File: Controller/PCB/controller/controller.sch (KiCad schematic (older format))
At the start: 8 parts

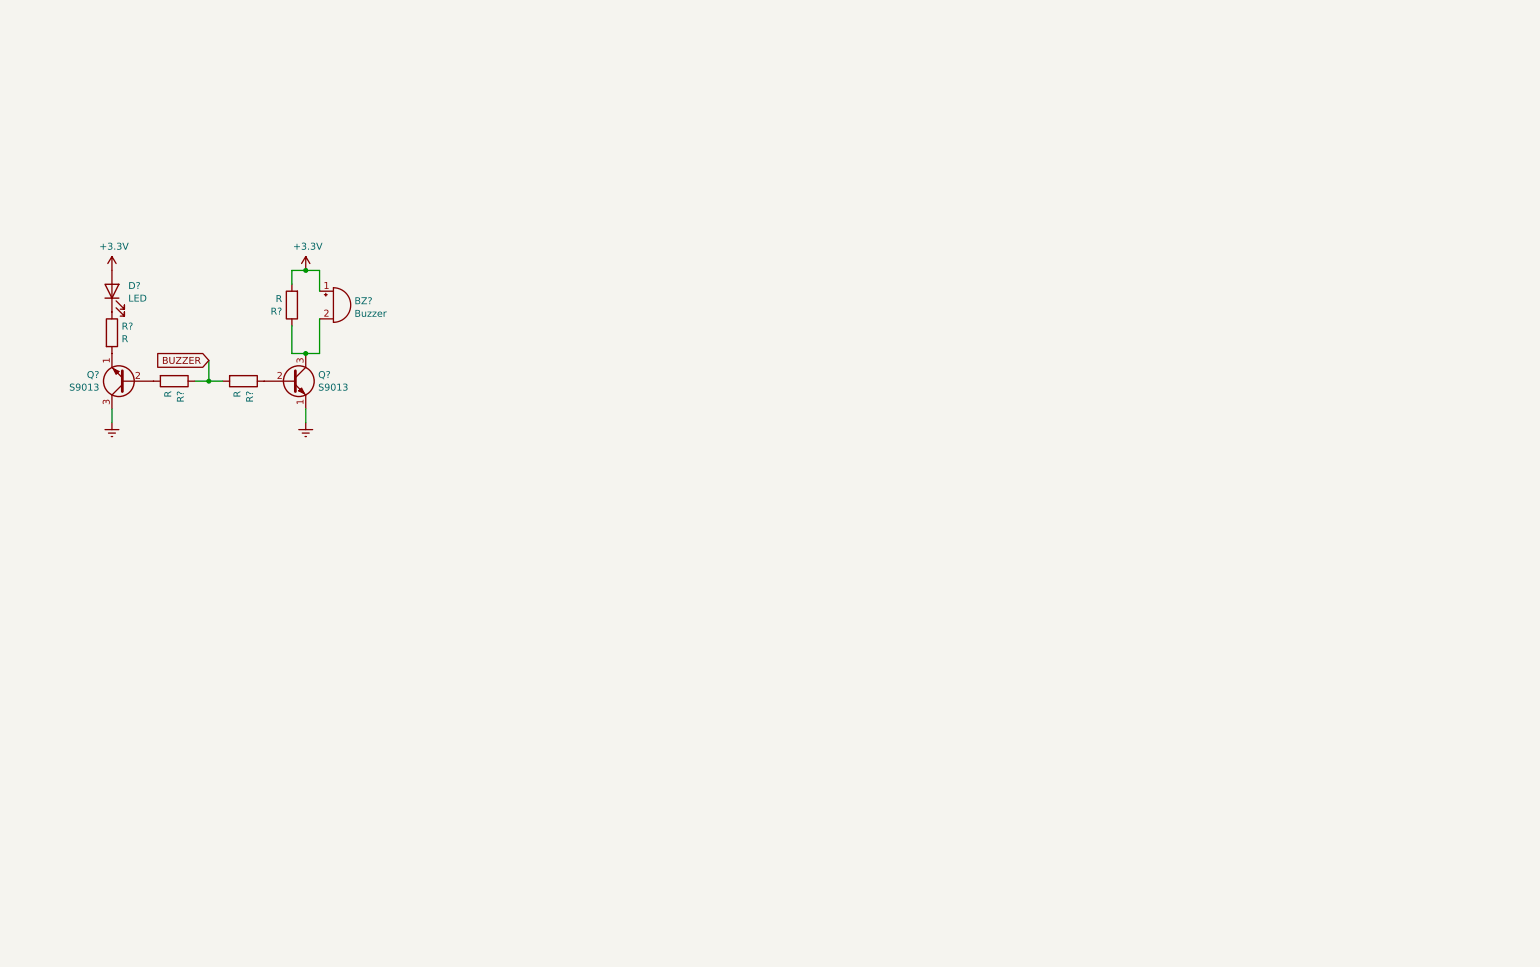
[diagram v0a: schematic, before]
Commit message: Add All inputs and Outputs to Circuit diagram
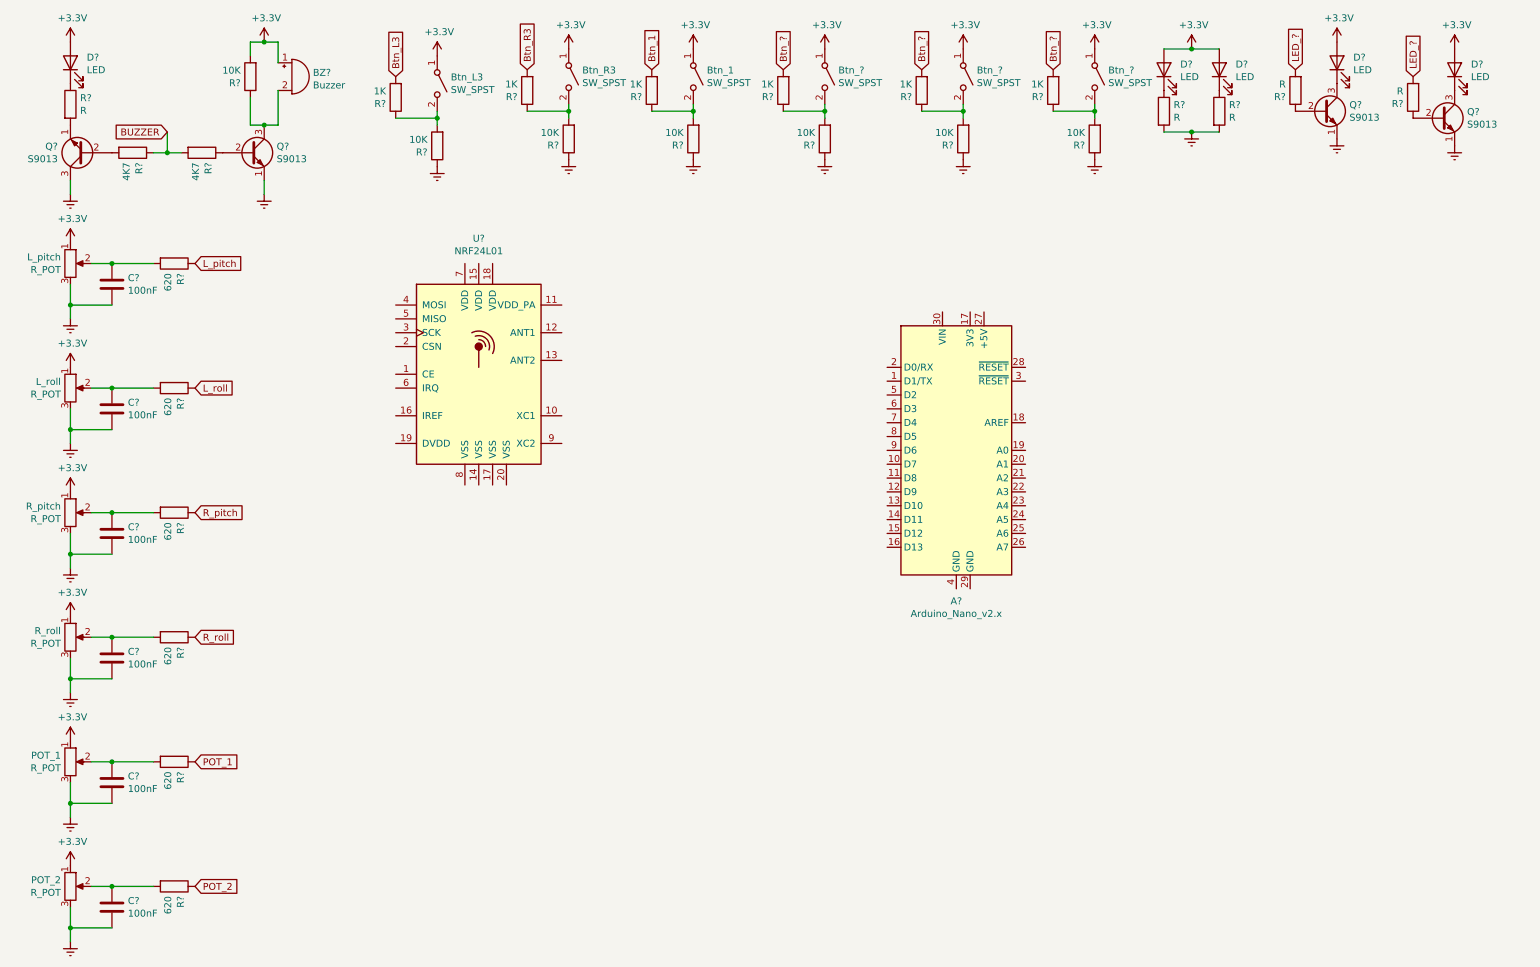
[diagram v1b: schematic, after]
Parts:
- added A?: Arduino_Nano_v2.x, Module:Arduino_Nano, symbol MCU_Module:Arduino_Nano_v2.x
- added Btn_1, Btn_? (x3), Btn_L3, Btn_R3: SW_SPST, symbol Switch:SW_SPST
- added C? (x6): 100nF, symbol Device:C
- added D? (x4): LED, symbol Device:LED
- added L_pitch, L_roll, POT_1, POT_2, R_pitch, R_roll: R_POT, symbol Device:R_POT
- added Q? (x2): S9013, Package_TO_SOT_THT:TO-39-3, symbol Transistor_BJT:2N2219
- added R? (x6): 620, symbol Device:R
- added R? (x6): 1K, symbol Device:R
- added R? (x6): 10K, symbol Device:R
- added R? (x4): R, symbol Device:R
- added U?: NRF24L01, Package_DFN_QFN:QFN-20-1EP_4x4mm_P0.5mm_EP2.5x2.5mm, symbol RF:NRF24L01
- R? (x2): value R -> 4K7
- R?: value R -> 10K
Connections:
- net +3V3: now also Btn_1.1 (A), Btn_?.1 (A), Btn_?.1 (A), Btn_?.1 (A), Btn_L3.1 (A), Btn_R3.1 (A), D?.2 (A), D?.2 (A), D?.2 (A), D?.2 (A), L_pitch.1, L_roll.1, POT_1.1, POT_2.1, R_pitch.1, R_roll.1
- net Earth: now also C?.2, C?.2, C?.2, C?.2, C?.2, C?.2, L_pitch.3, L_roll.3, POT_1.3, POT_2.3, Q?.1 (E), Q?.1 (E), R?.1, R?.1, R?.1, R?.1, R?.1, R?.1, R?.2, R?.2, R_pitch.3, R_roll.3
- new net: C?.1, L_pitch.2, R?.2
- new net: C?.1, L_roll.2, R?.2
- new net: C?.1, R?.2, R_pitch.2
- new net: C?.1, R?.2, R_roll.2
- new net: C?.1, POT_1.2, R?.2
- new net: C?.1, POT_2.2, R?.2
- new net: Btn_L3.2 (B), R?.1, R?.2
- new net: Btn_R3.2 (B), R?.1, R?.2
- new net: Btn_1.2 (B), R?.1, R?.2
- new net: Btn_?.2 (B), R?.1, R?.2 (x3)
- new net: D?.1 (K), R?.1 (x2)
- new net: D?.1 (K), Q?.3 (C) (x2)
- new net: Q?.2 (B), R?.1 (x2)
- new net Btn_1: R?.2
- new net Btn_?: R?.2, R?.2, R?.2
- new net Btn_L3: R?.2
- new net Btn_R3: R?.2
- new net LED_?: R?.2, R?.2
- new net L_pitch: R?.1
- new net L_roll: R?.1
- new net POT_1: R?.1
- new net POT_2: R?.1
- new net R_pitch: R?.1
- new net R_roll: R?.1
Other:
- moved on the sheet: BZ?, D?, Q?, R?

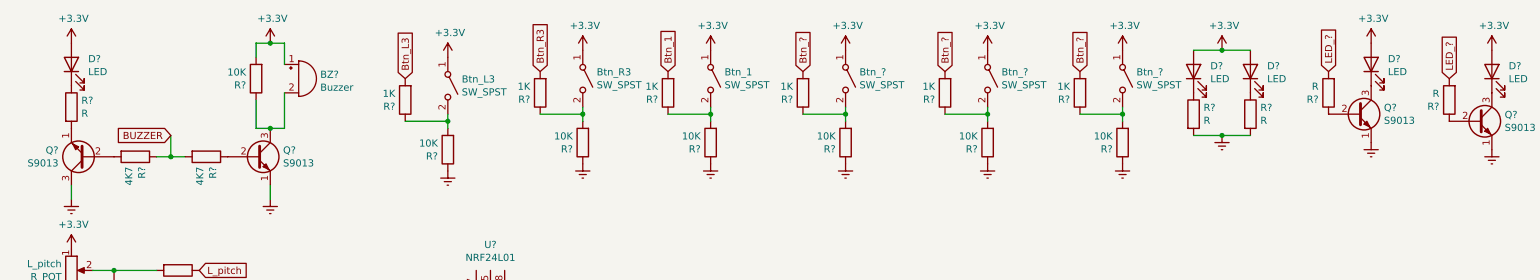
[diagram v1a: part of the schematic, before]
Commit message: Add Resistor Vals to the LEDs
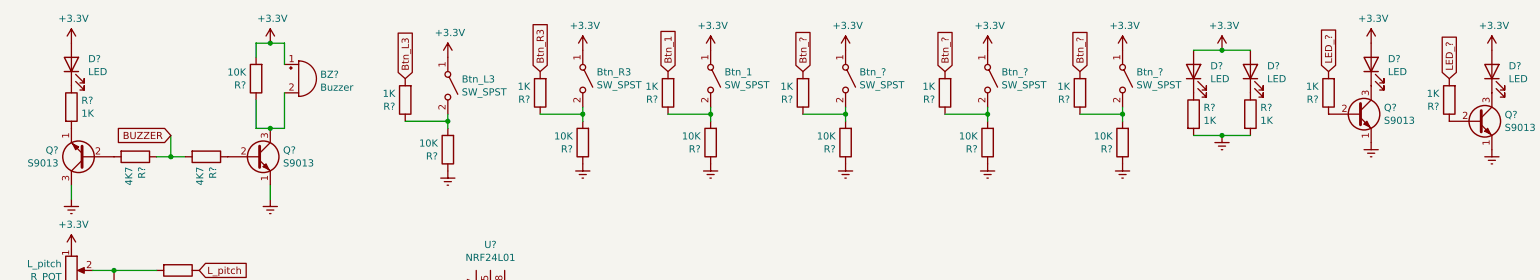
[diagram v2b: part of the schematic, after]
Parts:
- R? (x5): value R -> 1K
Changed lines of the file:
@@
 P 850 1150
 F 0 "R?" H 920 1196 50  0000 L CNN
-F 1 "R" H 920 1105 50  0000 L CNN
+F 1 "1K" H 920 1105 50  0000 L CNN
 F 2 "" V 780 1150 50  0001 C CNN
 F 3 "~" H 850 1150 50  0001 C CNN
@@
 P 8750 1200
 F 0 "R?" H 8820 1246 50  0000 L CNN
-F 1 "R" H 8820 1155 50  0000 L CNN
+F 1 "1K" H 8820 1155 50  0000 L CNN
 F 2 "" V 8680 1200 50  0001 C CNN
 F 3 "~" H 8750 1200 50  0001 C CNN
@@
 P 9150 1200
 F 0 "R?" H 9220 1246 50  0000 L CNN
-F 1 "R" H 9220 1155 50  0000 L CNN
+F 1 "1K" H 9220 1155 50  0000 L CNN
 F 2 "" V 9080 1200 50  0001 C CNN
 F 3 "~" H 9150 1200 50  0001 C CNN
@@
 P 9700 1050
 F 0 "R?" H 9770 1096 50  0000 L CNN
-F 1 "R" H 9770 1005 50  0000 L CNN
+F 1 "1K" H 9770 1005 50  0000 L CNN
 F 2 "" V 9630 1050 50  0001 C CNN
 F 3 "~" H 9700 1050 50  0001 C CNN
@@
 P 10550 1100
 F 0 "R?" H 10620 1146 50  0000 L CNN
-F 1 "R" H 10620 1055 50  0000 L CNN
+F 1 "1K" H 10620 1055 50  0000 L CNN
 F 2 "" V 10480 1100 50  0001 C CNN
 F 3 "~" H 10550 1100 50  0001 C CNN

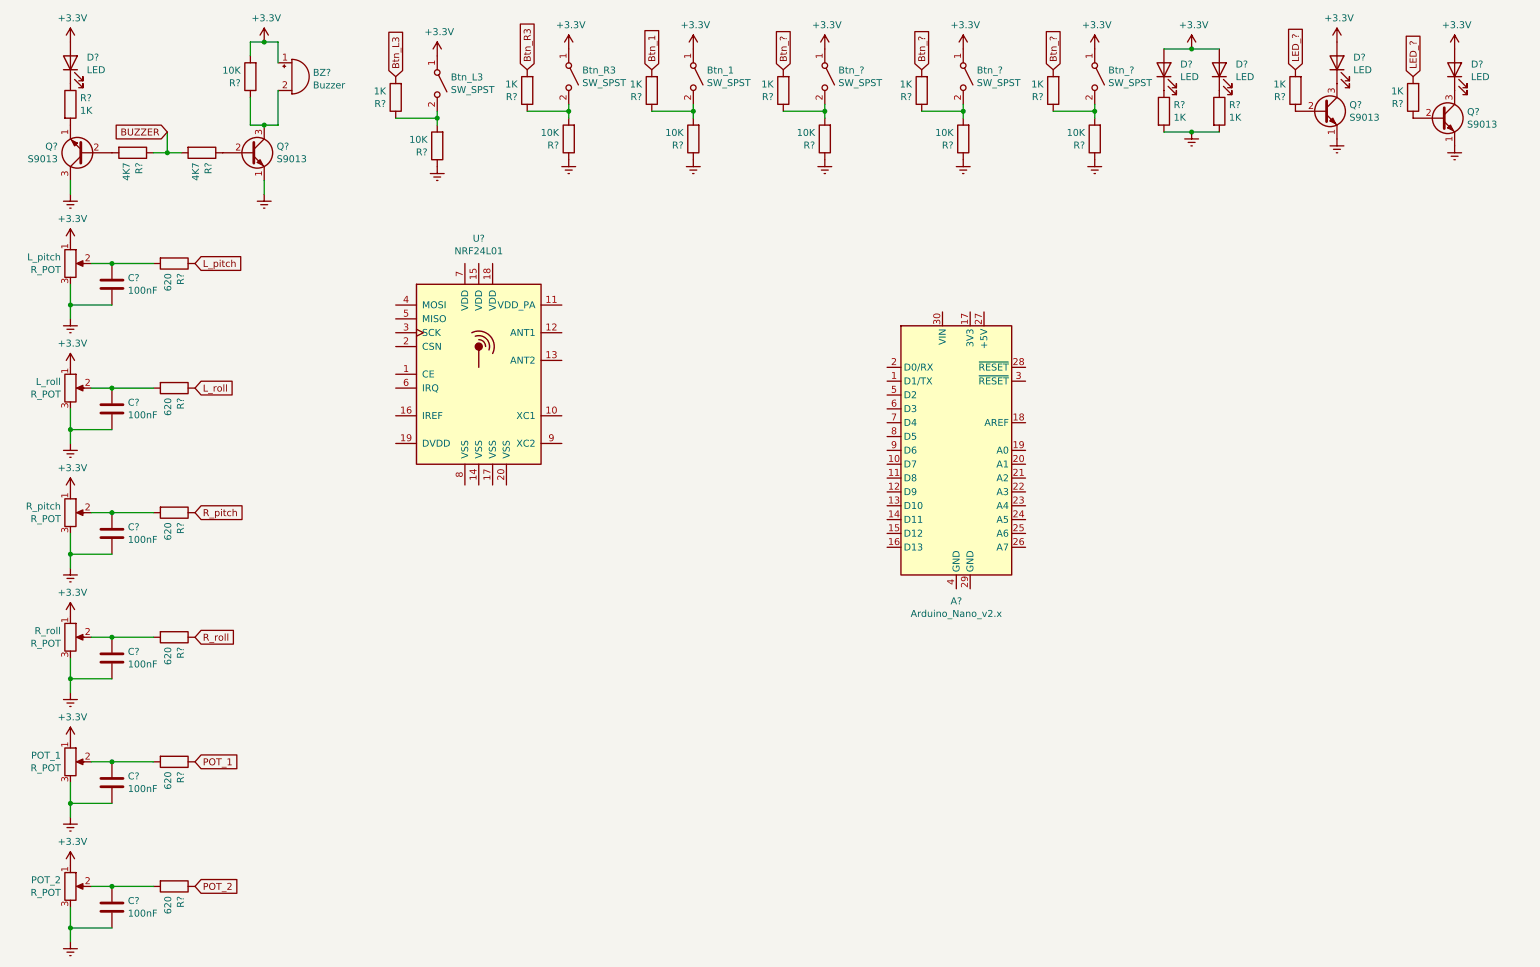
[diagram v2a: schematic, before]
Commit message: Add component pinouts and battery and voltage regulator
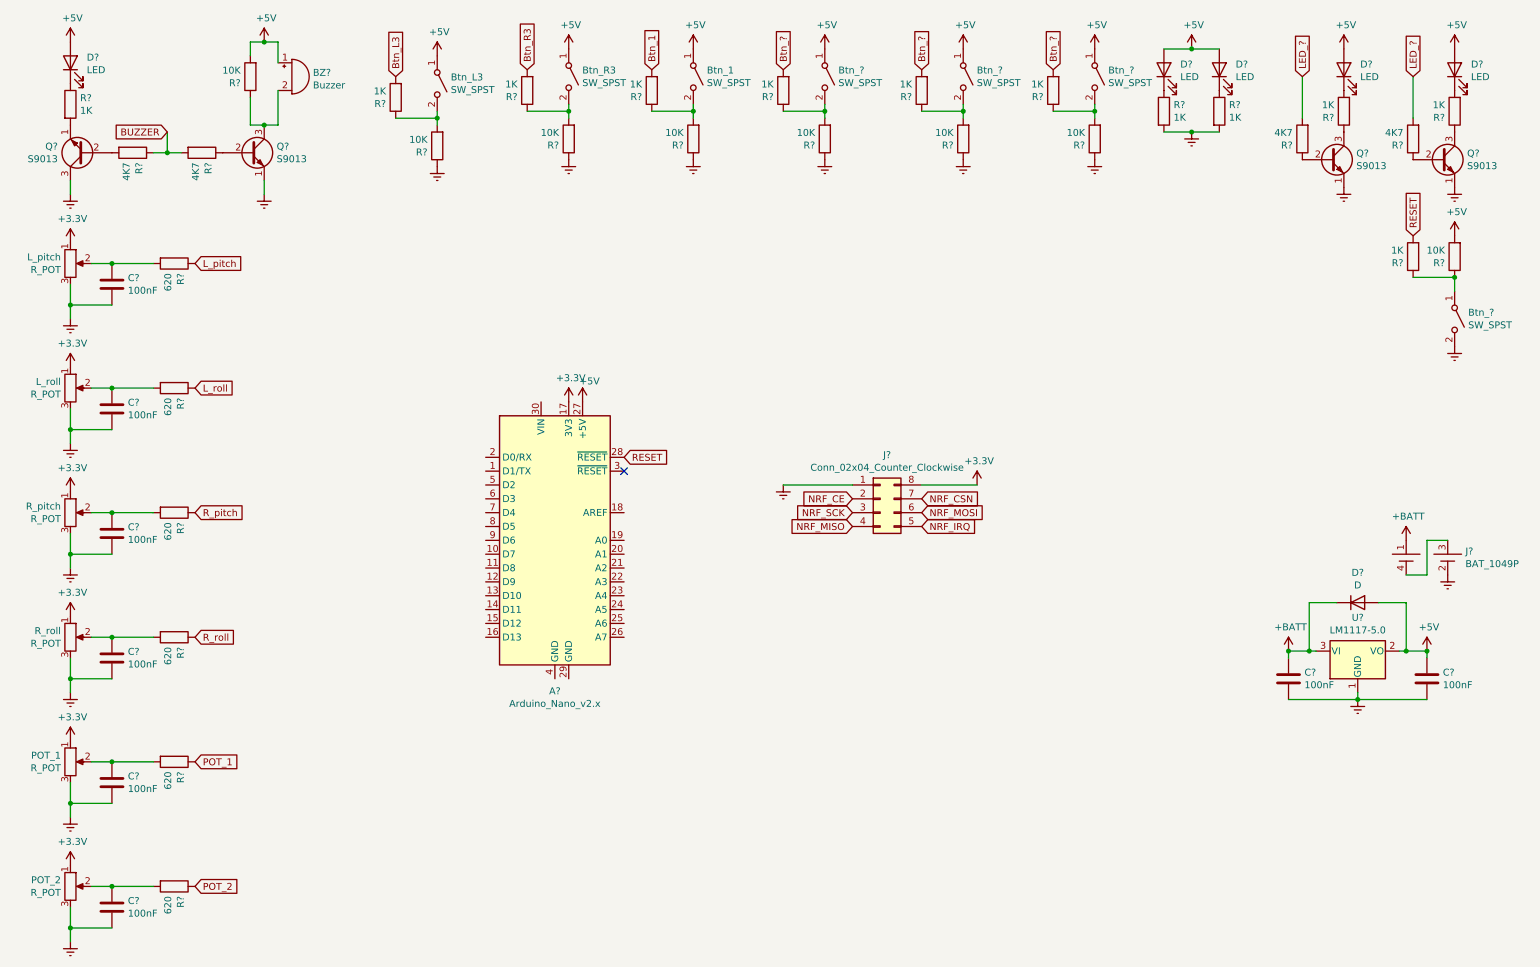
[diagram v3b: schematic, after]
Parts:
- removed D?: LED, symbol Device:LED
- removed Q?: S9013, Package_TO_SOT_THT:TO-39-3, symbol Transistor_BJT:2N2219
- removed R?: 1K, symbol Device:R
- removed U?: NRF24L01, Package_DFN_QFN:QFN-20-1EP_4x4mm_P0.5mm_EP2.5x2.5mm, symbol RF:NRF24L01
- added Btn_?: SW_SPST, symbol Switch:SW_SPST
- added C? (x2): 100nF, symbol Device:C
- added D?: LED, symbol Device:LED
- added D?: D, symbol Device:D
- added J?: BAT_1049P, symbol TickerForge:BAT_1049P
- added J?: Conn_02x04_Counter_Clockwise, symbol Connector_Generic:Conn_02x04_Counter_Clockwise
- added Q?: S9013, Package_TO_SOT_THT:TO-39-3, symbol Transistor_BJT:2N2219
- added R? (x2): 4K7, symbol Device:R
- added R? (x2): 1K, symbol Device:R
- added R?: 10K, symbol Device:R
- added U?: LM1117-5.0, symbol Regulator_Linear:LM1117-5.0
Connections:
- net +3V3: now also A?.17 (3V3), J?.8 (Pin_8); no longer BZ?.1 (-), Btn_1.1 (A), Btn_?.1 (A), Btn_?.1 (A), Btn_?.1 (A), Btn_L3.1 (A), Btn_R3.1 (A), D?.2 (A), D?.2 (A), D?.2 (A), D?.2 (A), R?.2
- net Earth: now also Btn_?.2 (B), C?.2, C?.2, J?.1 (Pin_1), J?.2, Q?.1 (E), U?.1 (GND)
- net LED_?: now also R?.2, R?.2; no longer R?.2
- net +5V: now reaches A?.27 (+5V)
- net +5V: now also BZ?.1 (-), Btn_1.1 (A), Btn_?.1 (A), Btn_?.1 (A), Btn_?.1 (A), Btn_L3.1 (A), Btn_R3.1 (A), D?.2 (A), D?.2 (A), D?.2 (A), D?.2 (A), R?.2, C?.1, D?.2 (A), D?.2 (A), R?.2, U?.2 (VO)
- net RESET: now reaches A?.28 (~RESET)
- net RESET: now also R?.2
- net at D?.1 (K): now also R?.2; no longer Q?.3 (C)
- net at Q?.2 (B): now also R?.1; no longer R?.1
- new net: J?.3, J?.4
- new net: Q?.3 (C), R?.1 (x2)
- new net: D?.1 (K), R?.2
- new net: Q?.2 (B), R?.1
- new net: Btn_?.1 (A), R?.1, R?.1
- new net +BATT: C?.1, D?.1 (K), J?.1, U?.3 (VI)
- new net NRF_CE: J?.2 (Pin_2)
- new net NRF_CSN: J?.7 (Pin_7)
- new net NRF_IRQ: J?.5 (Pin_5)
- new net NRF_MISO: J?.4 (Pin_4)
- new net NRF_MOSI: J?.6 (Pin_6)
- new net NRF_SCK: J?.3 (Pin_3)
- no-connect marks 0 -> 1
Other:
- moved on the sheet: A?, Q?, R?
